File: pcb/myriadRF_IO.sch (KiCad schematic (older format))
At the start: 2 parts, among them J801 FX10B-80S/8-SV, U401 XC7Axxt-FGG484

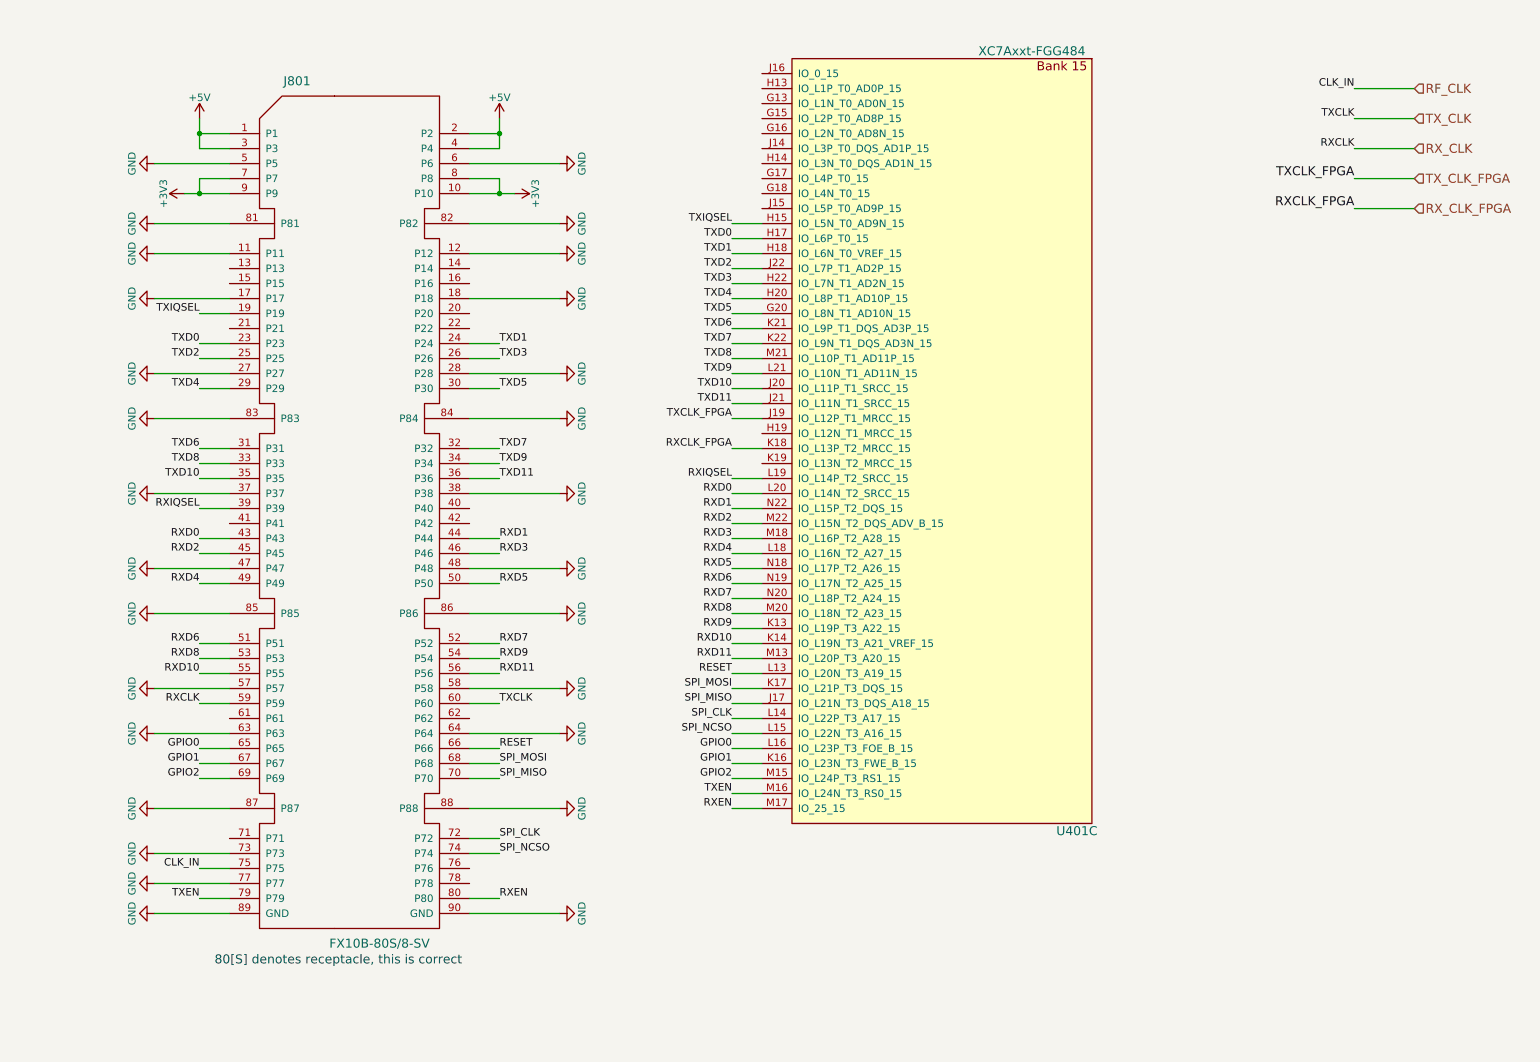
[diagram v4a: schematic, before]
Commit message: Finished most of the routing, removed DDR-3
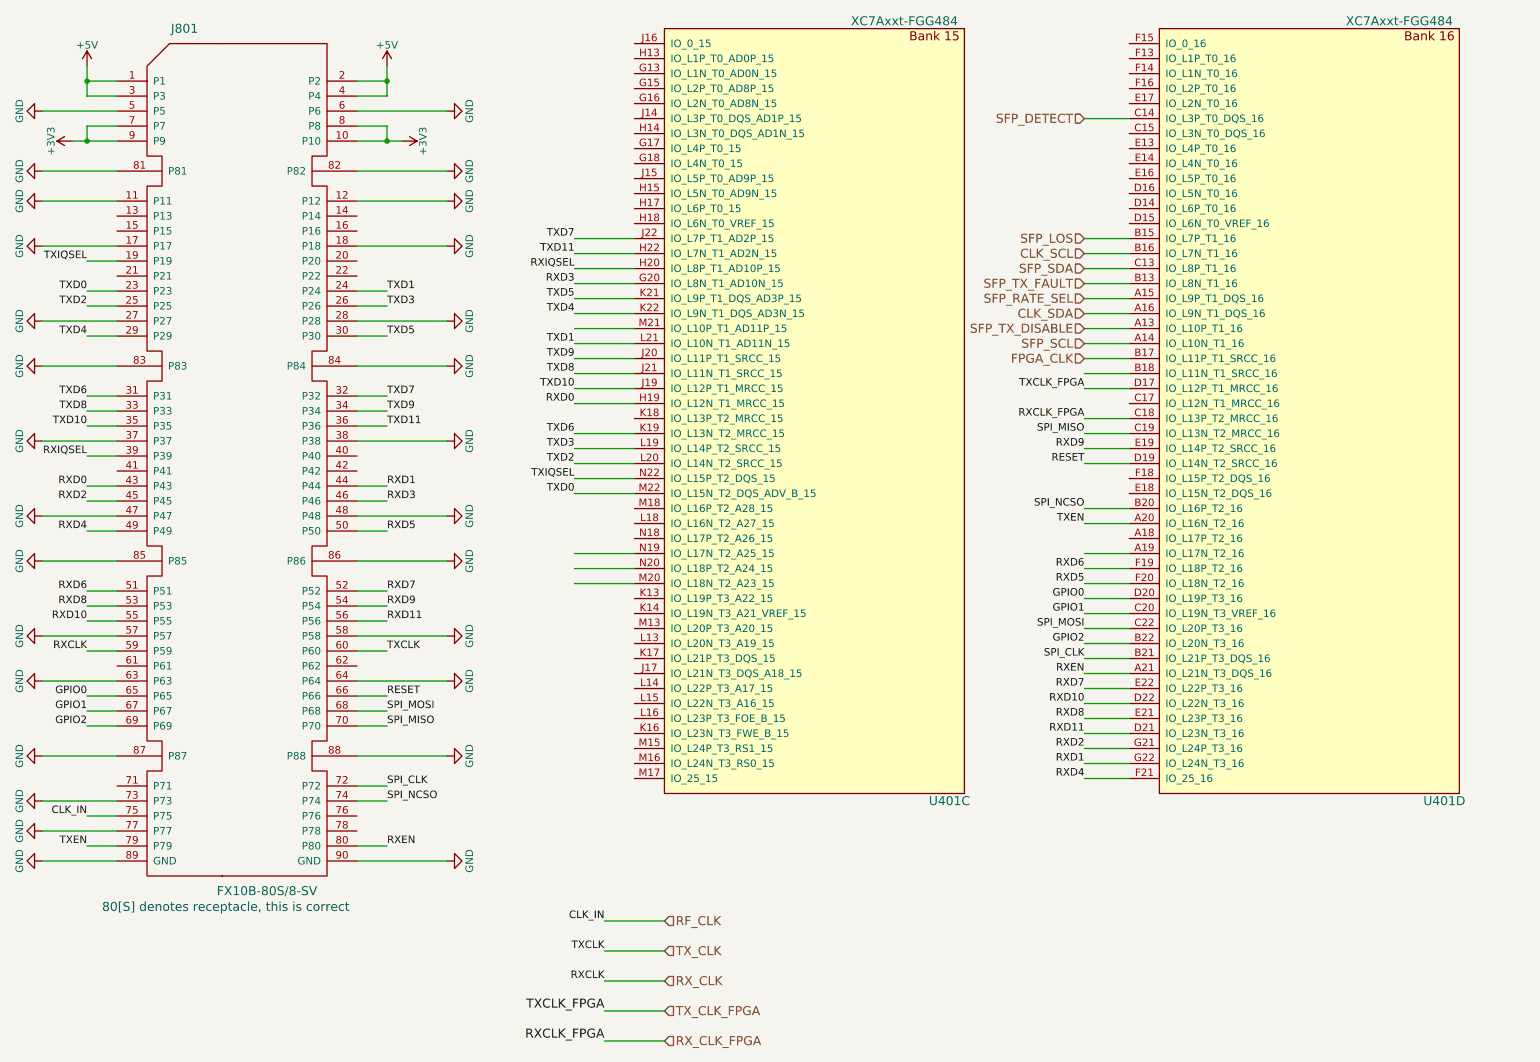
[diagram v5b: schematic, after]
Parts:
- added unit 4 of U401
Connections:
- net labels added: CLK_SCL, CLK_SDA, FPGA_CLK, SFP_DETECT, SFP_LOS, SFP_RATE_SEL, SFP_SCL, SFP_SDA, SFP_TX_DISABLE, SFP_TX_FAULT
- wire segments 122 -> 138
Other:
- moved on the sheet: J801, U401C

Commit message: Ready for fab
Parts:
- U401: symbol XC7Axxt-FGG484 -> XC7Axxt-FGG484-RESCUE-artix7_pcie_pcb
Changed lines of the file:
@@
 EESchema Schematic File Version 2
+LIBS:artix7_pcie_pcb-rescue
 LIBS:power
 LIBS:device
@@
 LIBS:valves
 LIBS:wbraun_ic_lib
-LIBS:pgmfoot
 LIBS:artix7_pcie_pcb-cache
 EELAYER 25 0
@@
 $EndComp
 $Comp
-L XC7Axxt-FGG484 U401
+L XC7Axxt-FGG484-RESCUE-artix7_pcie_pcb U401
 U 3 1 56341B2F
 P 6100 3450
@@
 RX_CLK_FPGA
 $Comp
-L XC7Axxt-FGG484 U401
+L XC7Axxt-FGG484-RESCUE-artix7_pcie_pcb U401
 U 4 1 56665963
 P 9400 3450
